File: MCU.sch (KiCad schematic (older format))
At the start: 8 parts, among them J1 ICSP Header, SW1 SW_SPST, U4 ATtiny84A-PU, Y1 8Mhz

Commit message: added additional IO expanders
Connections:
- net labels added: CH1_VOLT_SENSE, CH2_VOLT_SENSE
- wire segments 39 -> 41
- no-connect marks 0 -> 3
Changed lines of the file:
@@
 Text GLabel 6600 2450 2    50   Input ~ 0
 AREF
+Text GLabel 6600 2550 2    50   Input ~ 0
+CH1_VOLT_SENSE
+Text GLabel 6600 2650 2    50   Input ~ 0
+CH2_VOLT_SENSE
+Wire Wire Line
+	6150 2550 6600 2550
+Wire Wire Line
+	6150 2650 6600 2650
+NoConn ~ 6150 2750
+NoConn ~ 6150 3150
+NoConn ~ 6150 3550
 $EndSCHEMATC

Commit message: added digital pots for voltage control
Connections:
- net labels added: V1SET_SS, V2SET_SS
- wire segments 41 -> 43
- no-connect marks 3 -> 1
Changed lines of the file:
@@
 Wire Wire Line
 	6150 2650 6600 2650
-NoConn ~ 6150 2750
-NoConn ~ 6150 3150
 NoConn ~ 6150 3550
+Wire Wire Line
+	6150 3150 6600 3150
+Text GLabel 6600 2750 2    50   Input ~ 0
+V1SET_SS
+Text GLabel 6600 3150 2    50   Input ~ 0
+V2SET_SS
+Wire Wire Line
+	6150 2750 6600 2750
 $EndSCHEMATC

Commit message: Switched the MCU to a basic STM32, changed the business logic to 3V3, created a new 3V3 regulator for this. Also initialised code base. We'll use ARM Mbed for rapid development
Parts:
- removed C4: 0.1uF, symbol Device:C
- removed C5, C6: 22pF, symbol Device:C
- removed J1: ICSP Header, Connector_PinHeader_2.54mm:PinHeader_2x03_P2.54mm_Vertical, symbol Connector_Generic:Conn_02x03_Odd_Even
- removed U4: ATtiny84A-PU, Package_DIP:DIP-14_W7.62mm, symbol MCU_Microchip_ATtiny:ATtiny84A-PU
- removed Y1: 8Mhz, symbol Device:Crystal
- added C20: 4.7uF, symbol Device:CP
- added C21, C22, C23, C24: 0.1uF, symbol Device:C
- added J2: STLinkV2, symbol Connector_Generic:Conn_02x05_Odd_Even
- added U13: STM32F051K4Tx, Package_QFP:LQFP-32_7x7mm_P0.8mm, symbol MCU_ST_STM32F0:STM32F051K4Tx
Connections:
- net labels added: +3V3, I2C_SCL, I2C_SDA, PRG_SWCLK, PRG_SWDIO, PRG_SWIM, RESET, SPI_MISO, SPI_MOSI, SPI_SCK
- net labels removed: +5V, AREF, MISO, MOSI_SDA, RST, SCK_SCL
- wire segments 43 -> 74
- no-connect marks 1 -> 15
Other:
- moved on the sheet: R1, SW1

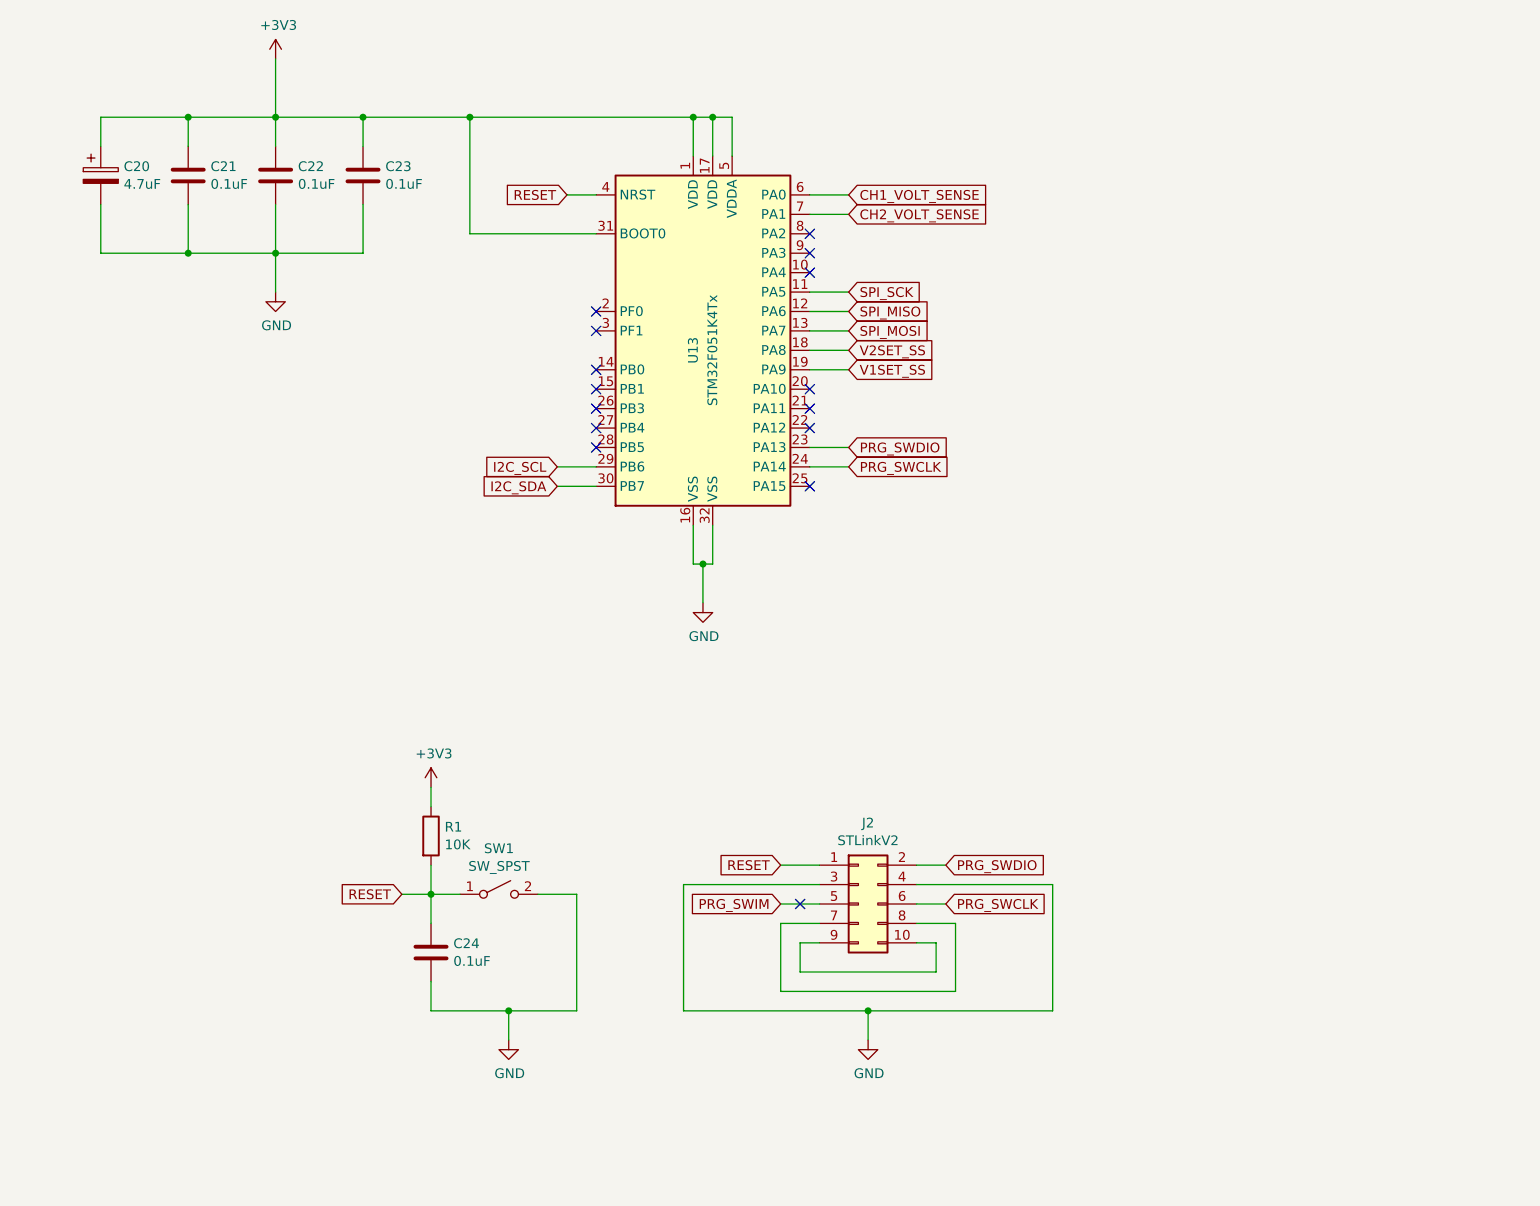
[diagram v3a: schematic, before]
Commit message: had to reload source files. Waiting on the STM32F01 so will compile for target STM32F303 for now. Just a temporary change for now
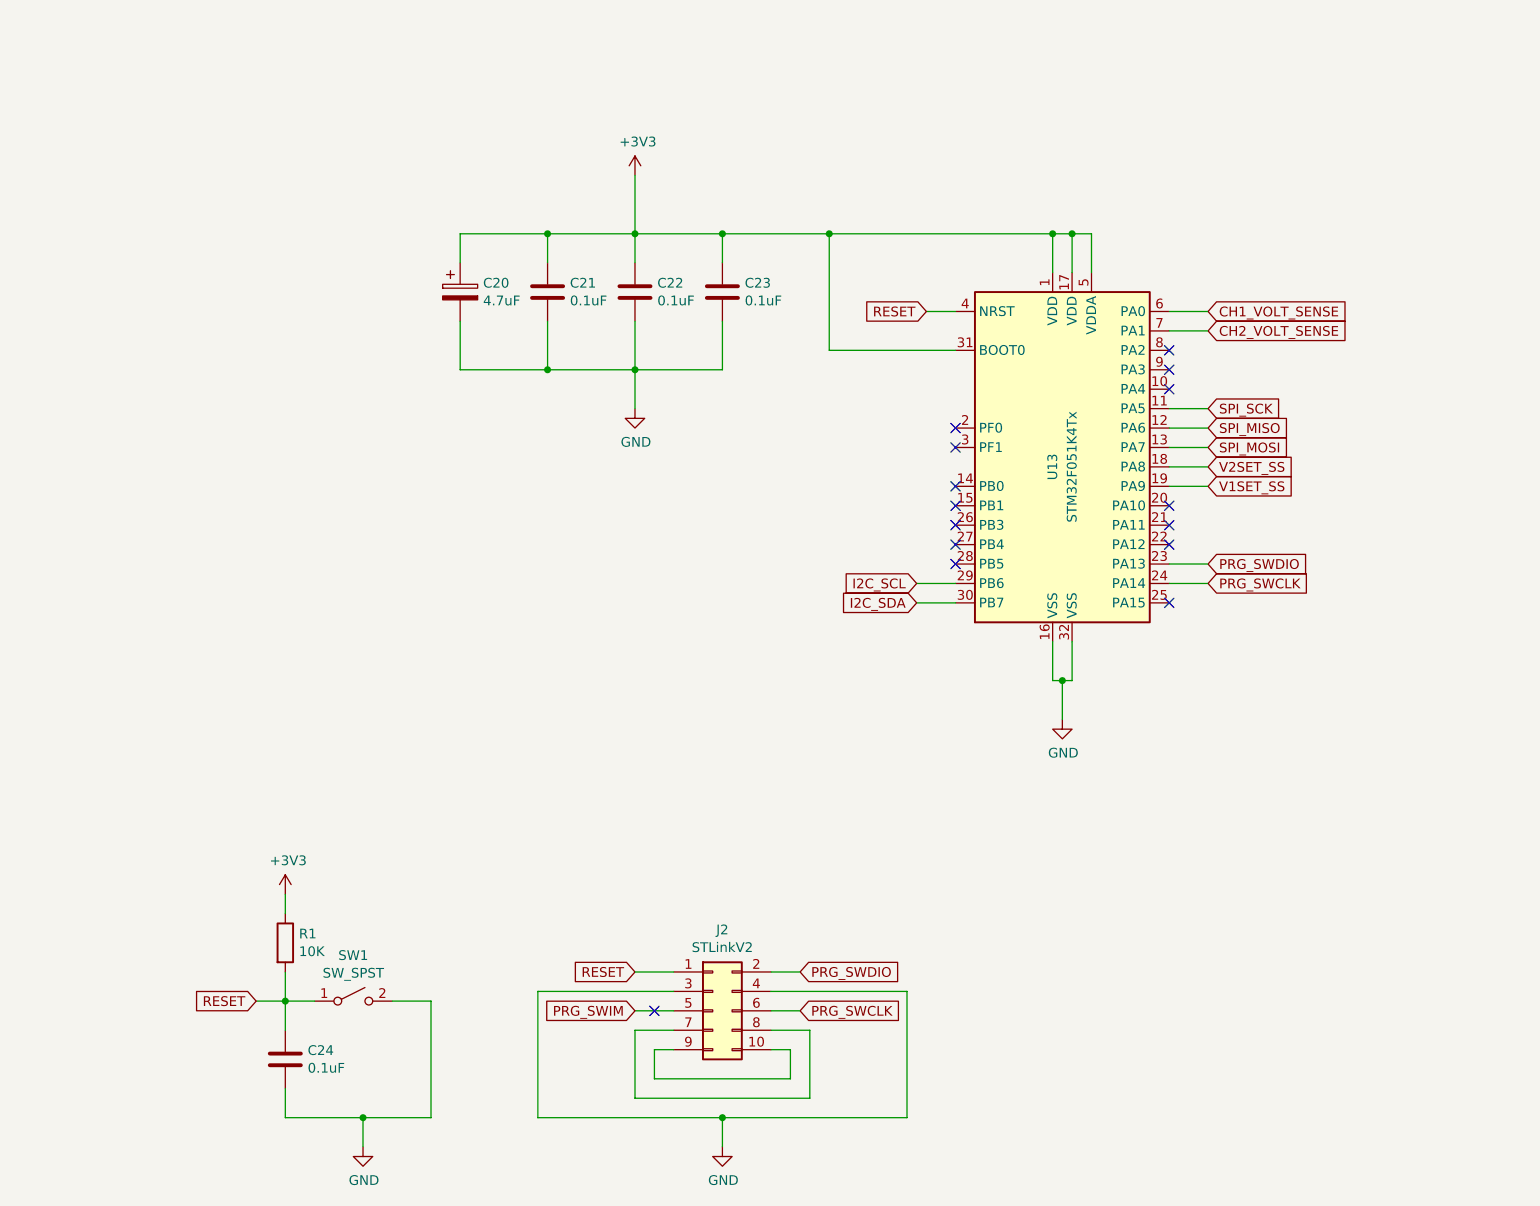
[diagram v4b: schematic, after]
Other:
- moved on the sheet: C20, C21, C22, C23, C24, J2, R1, SW1, U13

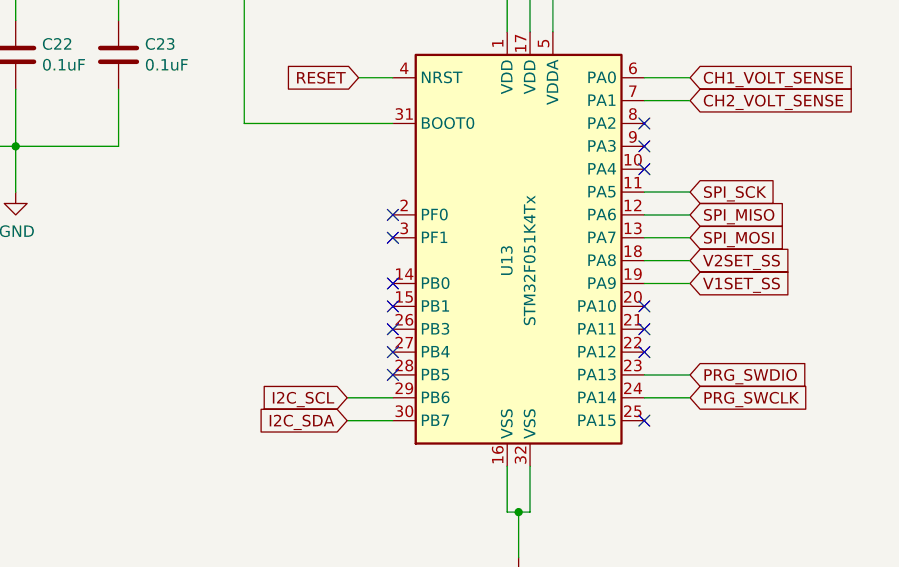
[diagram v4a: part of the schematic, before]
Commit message: We now have more MCU pins. Was able to remove two I2C IO expanders
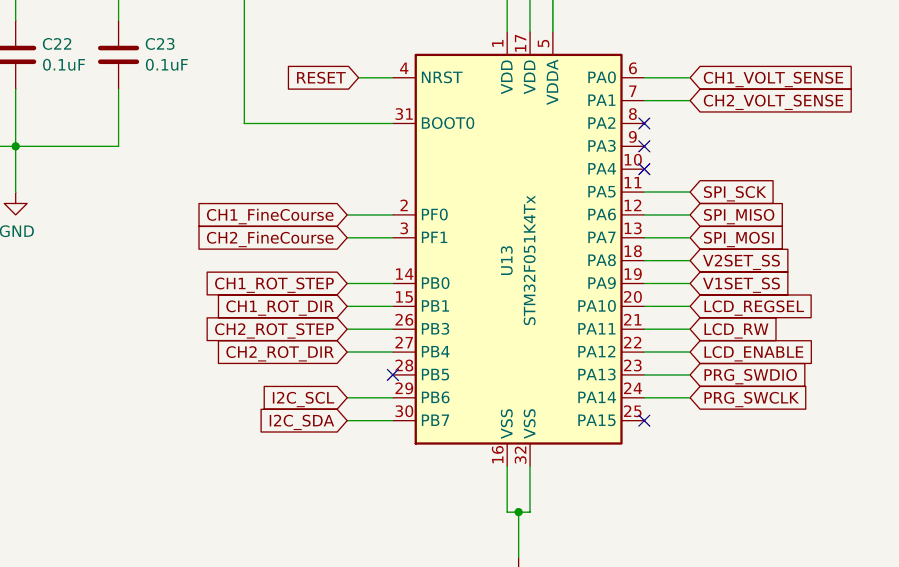
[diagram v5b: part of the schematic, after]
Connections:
- net CH1_ROT_STEP: now reaches U13.14 (PB0)
- net CH1_ROT_DIR: now reaches U13.15 (PB1)
- net CH1_FineCourse: now reaches U13.2 (PF0)
- net LCD_REGSEL: now reaches U13.20 (PA10)
- net LCD_RW: now reaches U13.21 (PA11)
- net LCD_ENABLE: now reaches U13.22 (PA12)
- net CH2_ROT_STEP: now reaches U13.26 (PB3)
- net CH2_ROT_DIR: now reaches U13.27 (PB4)
- net CH2_FineCourse: now reaches U13.3 (PF1)
- no-connect marks 15 -> 6
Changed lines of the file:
@@
 NoConn ~ 6850 2850
 NoConn ~ 6850 2950
-NoConn ~ 6850 3550
-NoConn ~ 6850 3650
-NoConn ~ 6850 3750
 NoConn ~ 6850 4050
 NoConn ~ 5750 3850
-NoConn ~ 5750 3750
-NoConn ~ 5750 3650
-NoConn ~ 5750 3550
-NoConn ~ 5750 3450
-NoConn ~ 5750 3250
-NoConn ~ 5750 3150
 Text GLabel 7050 3450 2    50   Input ~ 0
 V1SET_SS
@@
 Wire Wire Line
 	6850 3150 7050 3150
+Text GLabel 7050 3750 2    50   Input ~ 0
+LCD_ENABLE
+Text GLabel 7050 3650 2    50   Input ~ 0
+LCD_RW
+Text GLabel 7050 3550 2    50   Input ~ 0
+LCD_REGSEL
+Wire Wire Line
+	6850 3750 7050 3750
+Wire Wire Line
+	7050 3650 6850 3650
+Wire Wire Line
+	7050 3550 6850 3550
+Text GLabel 5550 3250 0    50   Input ~ 0
+CH2_FineCourse
+Text GLabel 5550 3150 0    50   Input ~ 0
+CH1_FineCourse
+Text GLabel 5550 3750 0    50   Input ~ 0
+CH2_ROT_DIR
+Text GLabel 5550 3550 0    50   Input ~ 0
+CH1_ROT_DIR
+Text GLabel 5550 3650 0    50   Input ~ 0
+CH2_ROT_STEP
+Text GLabel 5550 3450 0    50   Input ~ 0
+CH1_ROT_STEP
+Wire Wire Line
+	5550 3150 5750 3150
+Wire Wire Line
+	5550 3250 5750 3250
+Wire Wire Line
+	5550 3450 5750 3450
+Wire Wire Line
+	5550 3550 5750 3550
+Wire Wire Line
+	5550 3650 5750 3650
+Wire Wire Line
+	5550 3750 5750 3750
 $EndSCHEMATC

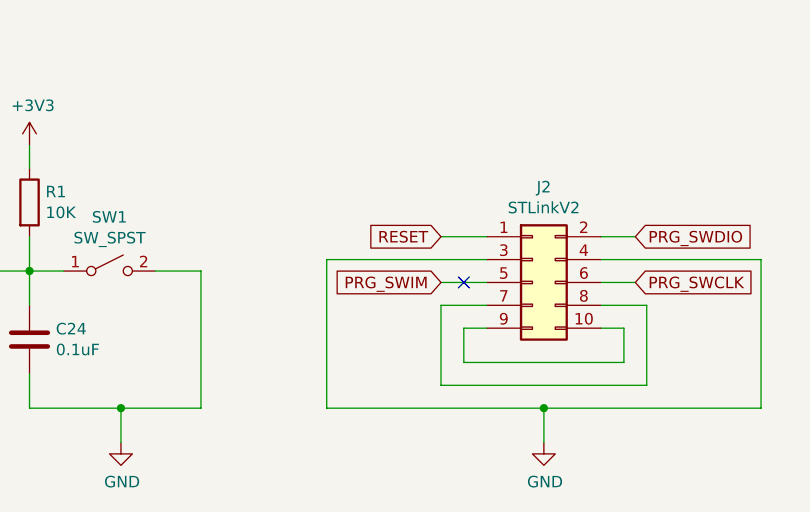
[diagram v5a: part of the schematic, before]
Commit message: fixed some DRC errors
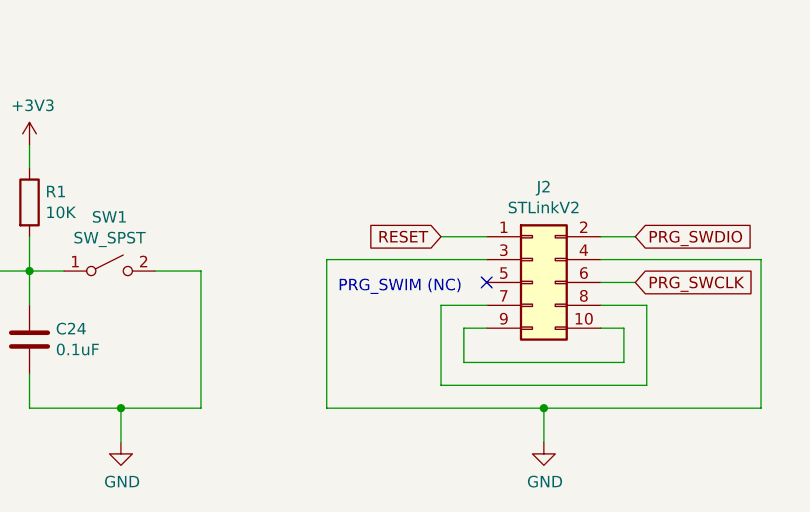
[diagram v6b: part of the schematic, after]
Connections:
- net PRG_SWIM: no longer names the net of J2.5 (Pin_5)
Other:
- note added: "PRG_SWIM (NC)"
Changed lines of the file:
@@
 Wire Wire Line
 	5000 6250 4800 6250
-Text GLabel 4100 6150 0    50   Input ~ 0
-PRG_SWIM
 $Comp
 L power:GND #PWR026
@@
 Wire Wire Line
 	4100 5950 4300 5950
-Wire Wire Line
-	4100 6150 4300 6150
 Wire Wire Line
 	4300 6050 3600 6050
@@
 Text GLabel 7050 3950 2    50   Input ~ 0
 PRG_SWCLK
-NoConn ~ 4200 6150
 Wire Wire Line
 	5750 3950 5550 3950
@@
 Wire Wire Line
 	5550 3750 5750 3750
+Text Notes 3650 6200 0    50   ~ 0
+PRG_SWIM (NC)
+NoConn ~ 4300 6150
 $EndSCHEMATC

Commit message: ported over LCD display code, modified schematic as we no longer need some of the I2C expanders
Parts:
- J2: footprint (none) -> Connector_PinHeader_2.54mm:PinHeader_2x05_P2.54mm_Vertical
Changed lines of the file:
@@
 F 0 "J2" H 4550 6567 50  0000 C CNN
 F 1 "STLinkV2" H 4550 6476 50  0000 C CNN
-F 2 "" H 4500 6150 50  0001 C CNN
+F 2 "Connector_PinHeader_2.54mm:PinHeader_2x05_P2.54mm_Vertical" H 4500 6150 50  0001 C CNN
 F 3 "~" H 4500 6150 50  0001 C CNN
 	1    4500 6150
